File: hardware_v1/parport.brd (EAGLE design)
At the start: 77.7 x 56 mm, 13 parts, among them IC1 74LS541DW, IC2 74LS541DW, IC3 74LS541DW, K1 PIN20X2

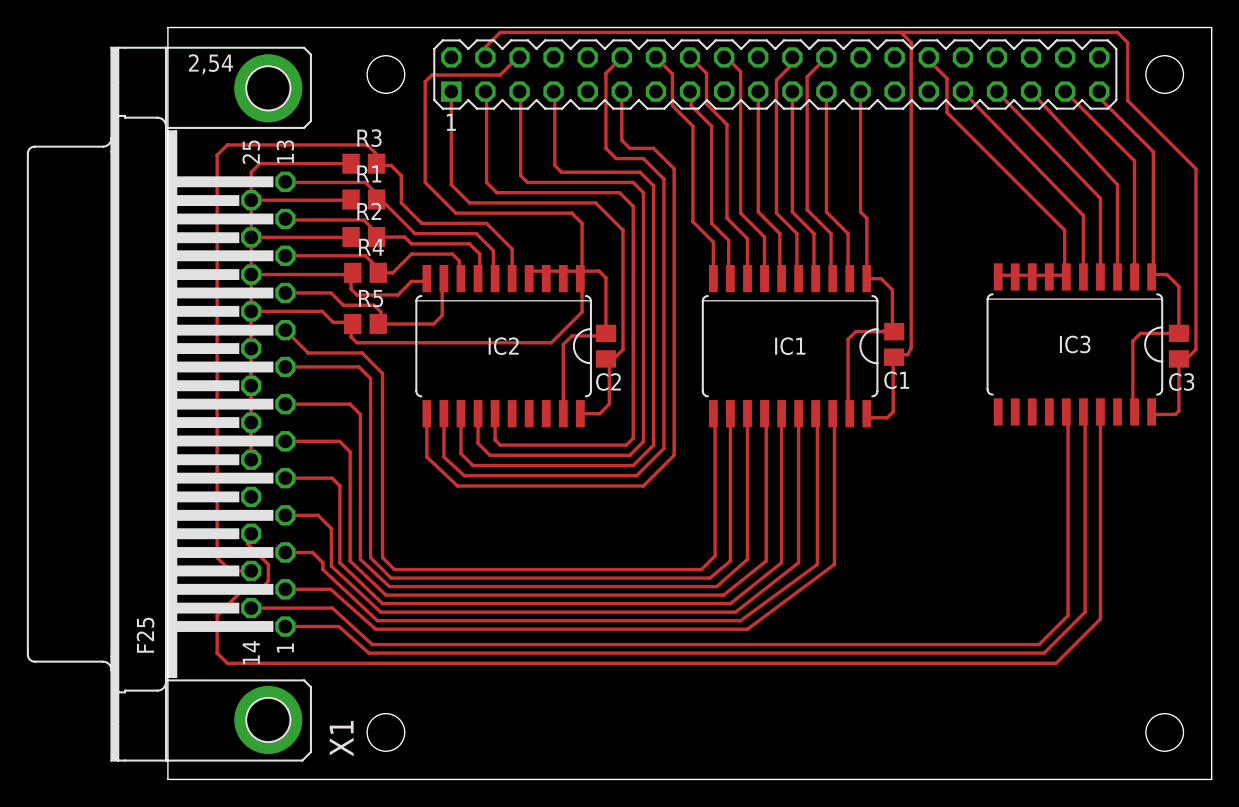
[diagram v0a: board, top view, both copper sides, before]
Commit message: hardware_v1: status 10k pd -> 4.3k pu
Change the 10K pulldowns to 4.3K pullups.
4.7K is what would normally be used here but I had some
803 4.3K's on hand.

Place some vias for the pullups and also for the unrouted
CONTROL3 line.  Before we had a one sided board which is
a bit easier to fab with the CNC.  Place vias so it can
still be made one sided without requiring connectors to
have plated through holes.  A small number of jumper wires
will need to be soldered to vias on aone sided board.
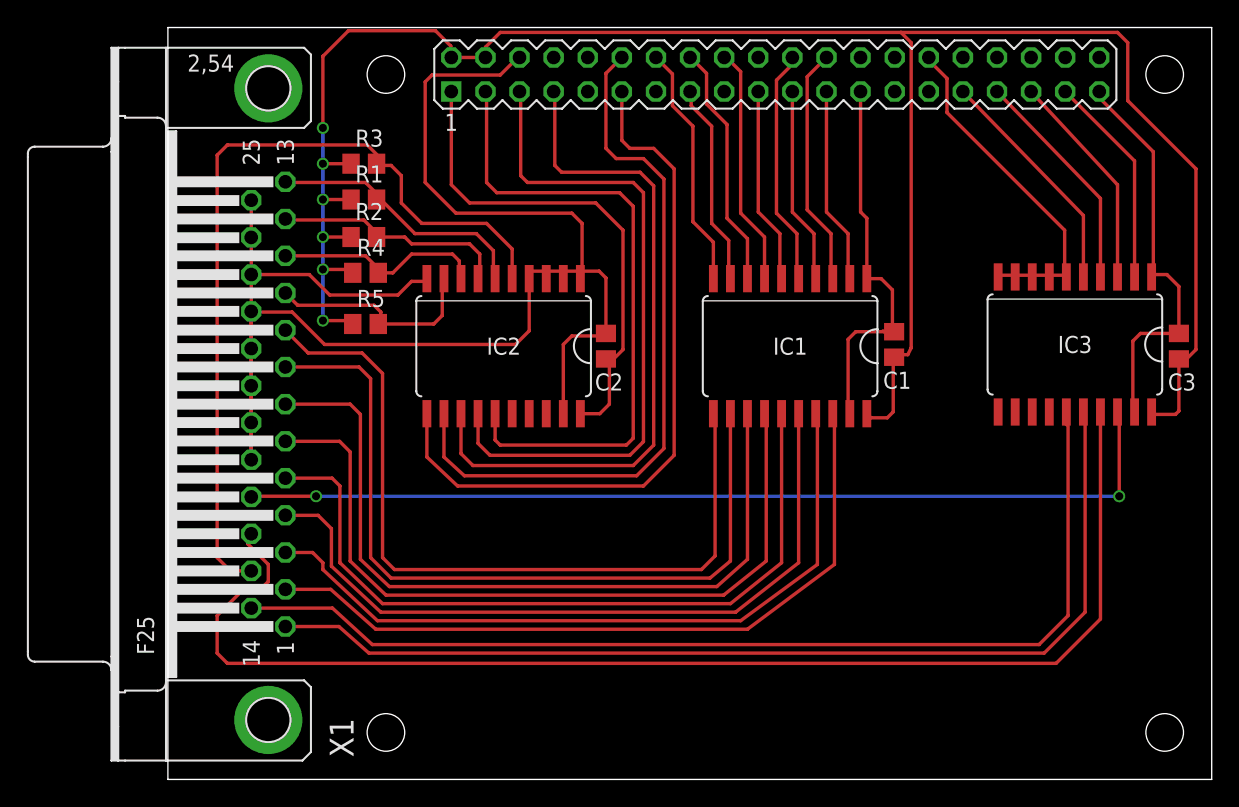
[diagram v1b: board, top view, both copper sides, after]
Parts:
- R1, R2, R3, R4, R5: value 10K -> 4.3K
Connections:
- net +5V: now also R1.1, R2.1, R3.1, R4.1, R5.1
- net GND: no longer R1.1, R2.1, R3.1, R4.1, R5.1
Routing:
- net CONTROL3: track 0.00 -> 71.1 mm, vias 0 -> 2
- net +5V: track 114.0 -> 159.1 mm, vias 0 -> 6
- net GND: track 255.2 -> 224.3 mm

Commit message: hardware_v1: replace DB25 with 2x13 header
It was a mistake to mount a DB25 directly on the adapter.
Use a 26 pin header and then off the shelf header to DB25
adapters can be used to suit the application.
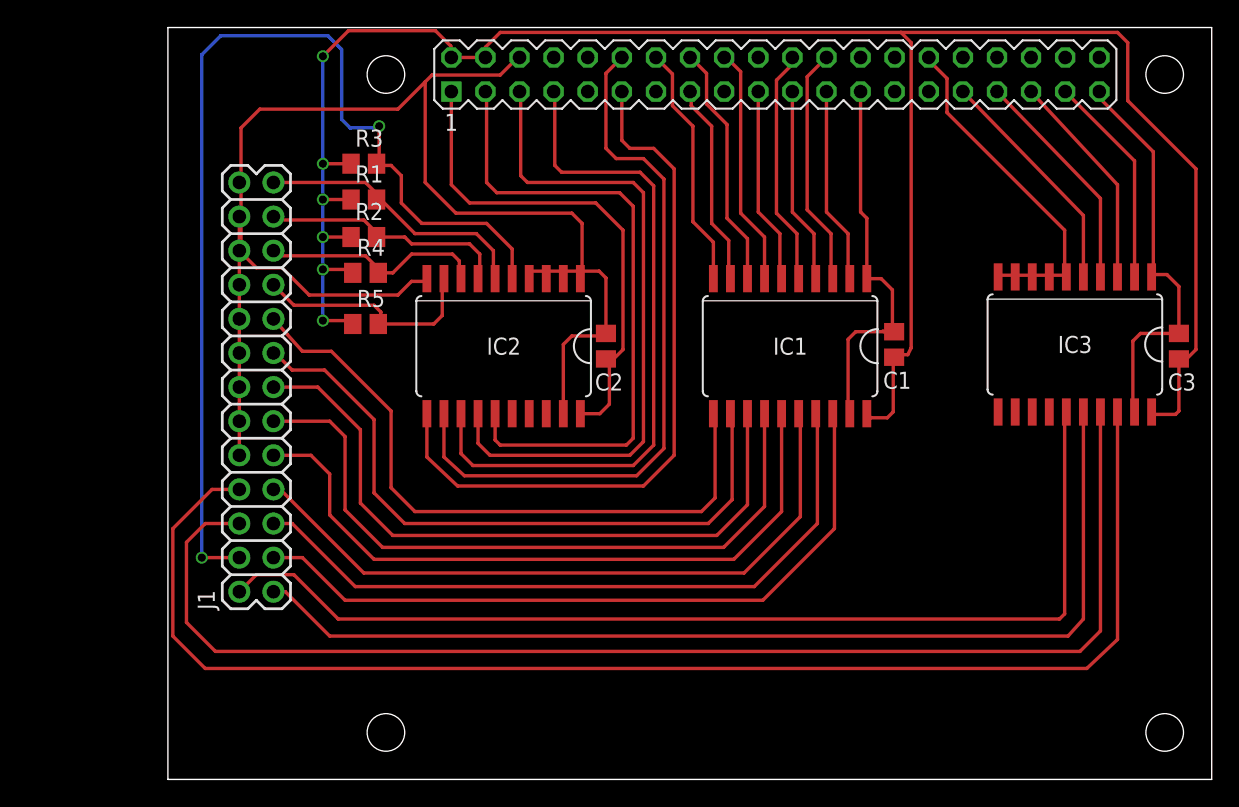
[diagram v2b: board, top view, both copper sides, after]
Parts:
- removed X1: (no value), con-subd:F25HP
- added J1: (no value), SparkFun-Connectors:2X13
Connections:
- net CONTROL0: now also J1.1; no longer X1.1
- net CONTROL1: now also J1.2; no longer X1.14
- net CONTROL2: now also J1.6; no longer X1.16
- net CONTROL3: now also J1.8; no longer X1.17
- net DATA0: now also J1.3; no longer X1.2
- net DATA1: now also J1.5; no longer X1.3
- net DATA2: now also J1.7; no longer X1.4
- net DATA3: now also J1.9; no longer X1.5
- net DATA4: now also J1.11; no longer X1.6
- net DATA5: now also J1.13; no longer X1.7
- net DATA6: now also J1.15; no longer X1.8
- net DATA7: now also J1.17; no longer X1.9
- net GND: now also J1.10, J1.12, J1.14, J1.16, J1.18, J1.20, J1.22, J1.24; no longer X1.18, X1.19, X1.20, X1.21, X1.22, X1.23, X1.24, X1.25, X1.G1, X1.G2
- net STATUS3: now also J1.4; no longer X1.15
- net STATUS4: now also J1.25; no longer X1.13
- net STATUS5: now also J1.23; no longer X1.12
- net STATUS6: now also J1.19; no longer X1.10
- net STATUS7: now also J1.21; no longer X1.11
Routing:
- net CONTROL3: track 71.1 -> 103.3 mm, vias 2 -> 0
- net STATUS3: track 61.6 -> 79.0 mm, vias 0 -> 2
- net GND: track 224.3 -> 212.1 mm
- net DATA6: track 58.9 -> 49.0 mm
- net DATA7: track 57.8 -> 49.0 mm
- net DATA5: track 58.0 -> 50.8 mm
- net DATA4: track 56.5 -> 51.8 mm
- net DATA3: track 56.1 -> 51.6 mm
- net DATA2: track 55.2 -> 51.3 mm
- net DATA1: track 54.6 -> 52.4 mm
- net CONTROL2: track 94.8 -> 96.4 mm
- net CONTROL1: track 77.3 -> 78.6 mm
- net STATUS6: track 16.5 -> 17.6 mm
- net CONTROL0: track 76.5 -> 77.7 mm
- net STATUS7: track 15.6 -> 16.7 mm
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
